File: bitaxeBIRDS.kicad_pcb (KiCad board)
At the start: 6 copper layers, 65 x 112 mm, 195 parts, among them J1 XT30, J2 USB_C_Receptacle_USB2.0, J3 Conn_01x04, J4 Conn_01x04, SW1 SWITCH-SPST, SW2 SWITCH-SPST, U1 TPSM861253RDXR, U12 TLV75512PDQNR, U13 EMC2103-2, U14 TLV75512PDQNR, U15 TLV75512PDQNR, U2 TPS546D24ARVFR, U3 TLV75512PDQNR, U4 W25Q16JVUXIQ TR, U5 TPS22919DCKR, U6 RP2040, U7 SK6812, U8 SN74AVC4T774, U9 Raspberry Pi Pico, Y1 12MHz, Y2 50MHz

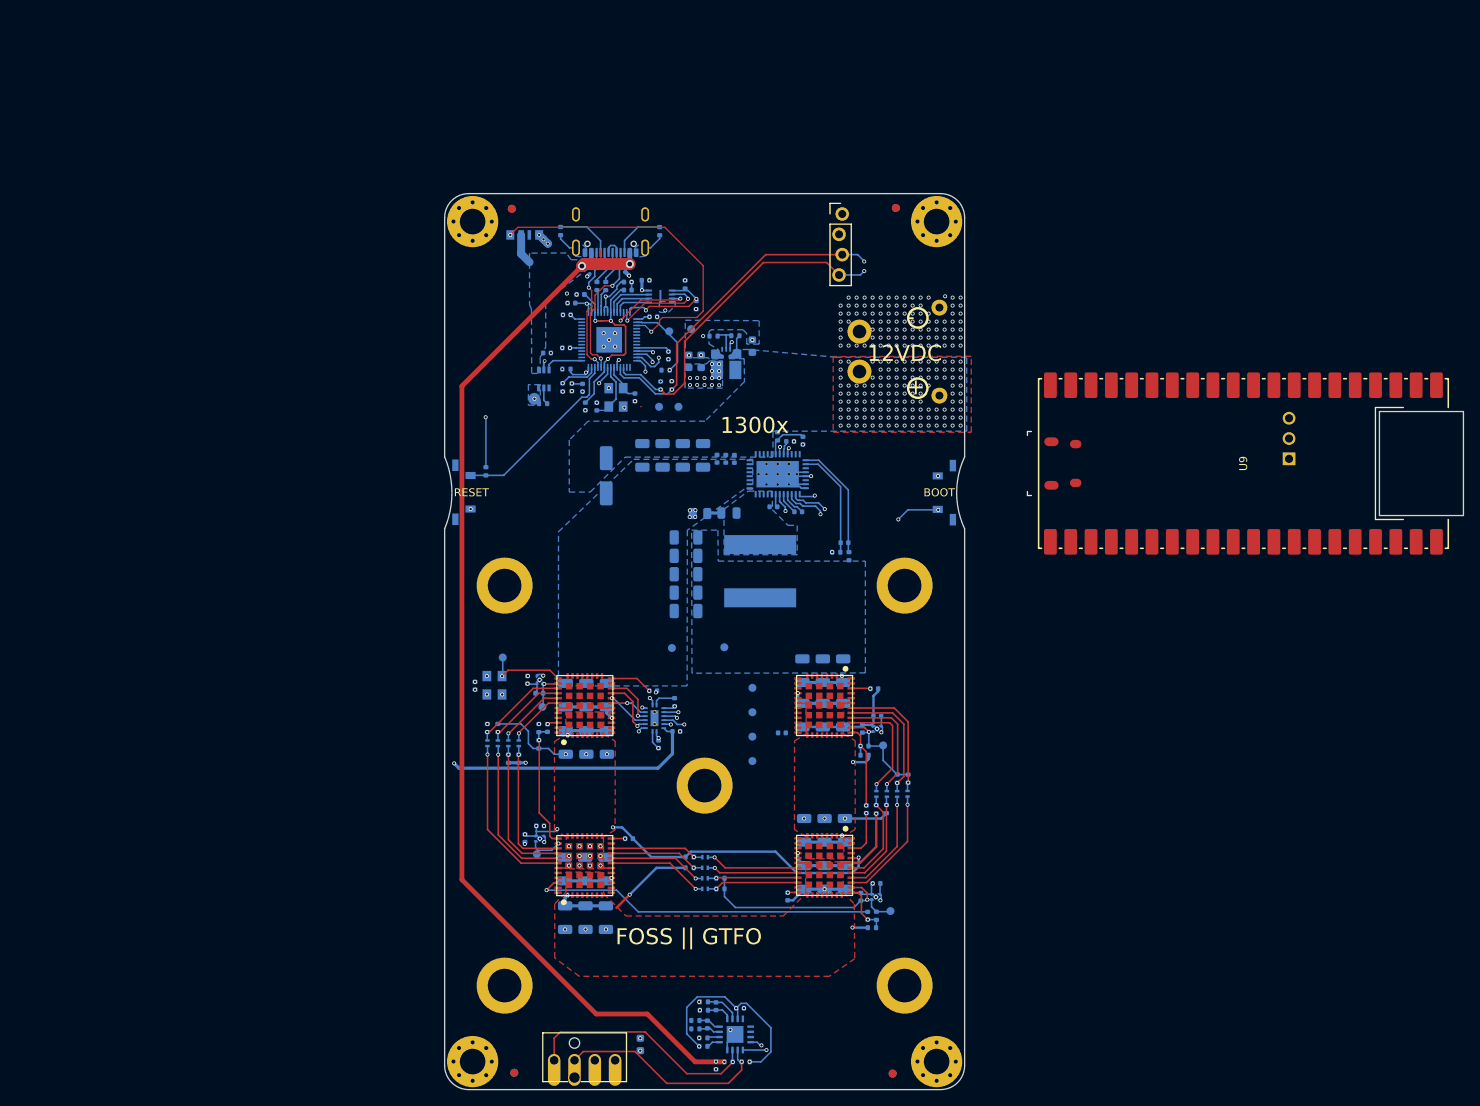
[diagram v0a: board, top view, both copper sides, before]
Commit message: switched to THT RPi Pico 2W style. Made 8mm taller.
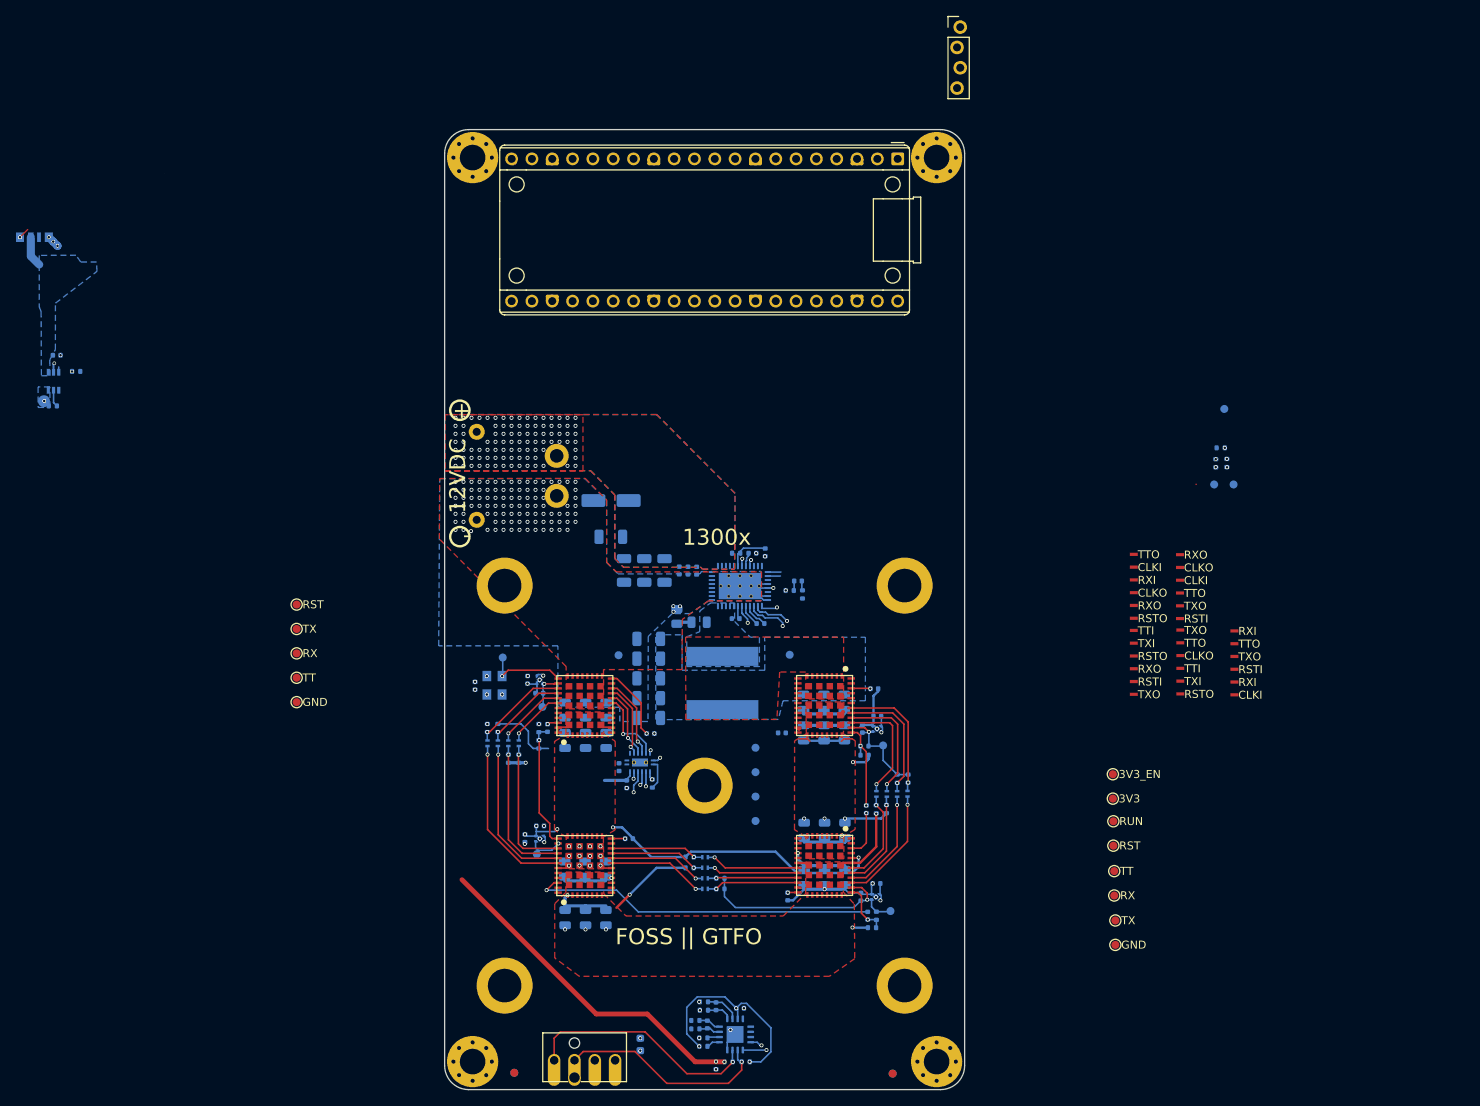
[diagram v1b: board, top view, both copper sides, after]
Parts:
- removed C1, C12, C8: 10uF, Capacitor_SMD:C_0603_1608Metric
- removed C42, C43: 30pF, Capacitor_SMD:C_0402_1005Metric
- removed C44, C46, C47, C50, C51, C52, C53, C54, C55, C56: 0.1uF, Capacitor_SMD:C_0402_1005Metric
- removed C48, C49: 1uF, Capacitor_SMD:C_0402_1005Metric
- removed J2: USB_C_Receptacle_USB2.0, aditBoard:USB_C_Receptacle_GCT_USB4105-xx-A_16P_TopMnt_Horizontal
- removed R1: 20k, Resistor_SMD:R_0402_1005Metric
- removed R15, R2, R4: 10k, Resistor_SMD:R_0402_1005Metric
- removed R16, R17: 5.1k, Resistor_SMD:R_0402_1005Metric
- removed R18: 1k, Resistor_SMD:R_0402_1005Metric
- removed R19: 49.9k, Resistor_SMD:R_0402_1005Metric
- removed R21, R22: 33, Resistor_SMD:R_0402_1005Metric
- removed SW1, SW2: SWITCH-SPST, bitaxe:SW_TL3330AF130QG_EWI
- removed U1: TPSM861253RDXR, bitaxe:TPSM863257RDX
- removed U4: W25Q16JVUXIQ TR, emberone:USON-8_UX_2x3x0p6_WIN
- removed U6: RP2040, Package_DFN_QFN:QFN-56-1EP_7x7mm_P0.4mm_EP3.2x3.2mm
- removed Y1: 12MHz, emberone:XTAL_ECS-120-20-33-CKM-TR3
- added TP15: 3V3, bitaxe:TestPoint_Pad_D1.0mm, F.Cu at (182.0, 113.6)
- added TP16: RUN, bitaxe:TestPoint_Pad_D1.0mm, F.Cu at (182.1, 116.5)
- added TP17: TX, bitaxe:TestPoint_Pad_D1.0mm, F.Cu at (80.0, 92.4)
- added TP20: RX, bitaxe:TestPoint_Pad_D1.0mm, F.Cu at (80.0, 95.5)
- added TP21: TT, bitaxe:TestPoint_Pad_D1.0mm, F.Cu at (80.0, 98.5)
- added TP22: GND, bitaxe:TestPoint_Pad_D1.0mm, F.Cu at (80.0, 101.6)
- added TP23: RST, bitaxe:TestPoint_Pad_D1.0mm, F.Cu at (182.1, 119.5)
- added TP24: TT, bitaxe:TestPoint_Pad_D1.0mm, F.Cu at (182.2, 122.7)
- added TP25: RX, bitaxe:TestPoint_Pad_D1.0mm, F.Cu at (182.2, 125.7)
- added TP26: TX, bitaxe:TestPoint_Pad_D1.0mm, F.Cu at (182.3, 128.9)
- added TP27: GND, bitaxe:TestPoint_Pad_D1.0mm, F.Cu at (182.3, 131.9)
- added TP28: TTI, bitaxe:TestPoint_Pad_1.0x0.4mm, F.Cu at (184.6, 92.6)
- added TP29: TXI, bitaxe:TestPoint_Pad_1.0x0.4mm, F.Cu at (184.6, 94.2)
- added TP30: RSTO, bitaxe:TestPoint_Pad_1.0x0.4mm, F.Cu at (184.6, 95.8)
- added TP31: RXO, bitaxe:TestPoint_Pad_1.0x0.4mm, F.Cu at (184.6, 97.4)
- added TP32: RSTI, bitaxe:TestPoint_Pad_1.0x0.4mm, F.Cu at (184.6, 99.0)
- added TP33: TXO, bitaxe:TestPoint_Pad_1.0x0.4mm, F.Cu at (184.6, 100.6)
- added TP34: TTO, bitaxe:TestPoint_Pad_1.0x0.4mm, F.Cu at (184.6, 83.1)
- added TP35: CLKI, bitaxe:TestPoint_Pad_1.0x0.4mm, F.Cu at (184.6, 84.7)
- added TP36: RXI, bitaxe:TestPoint_Pad_1.0x0.4mm, F.Cu at (184.6, 86.3)
- added TP37: CLKO, bitaxe:TestPoint_Pad_1.0x0.4mm, F.Cu at (184.6, 87.9)
- added TP38: RXO, bitaxe:TestPoint_Pad_1.0x0.4mm, F.Cu at (184.6, 89.5)
- added TP39: RSTO, bitaxe:TestPoint_Pad_1.0x0.4mm, F.Cu at (184.6, 91.1)
- added TP40: TXO, bitaxe:TestPoint_Pad_1.0x0.4mm, F.Cu at (190.5, 92.6)
- added TP41: TTO, bitaxe:TestPoint_Pad_1.0x0.4mm, F.Cu at (190.5, 94.2)
- added TP42: CLKO, bitaxe:TestPoint_Pad_1.0x0.4mm, F.Cu at (190.5, 95.7)
- added TP43: TTI, bitaxe:TestPoint_Pad_1.0x0.4mm, F.Cu at (190.5, 97.3)
- added TP44: TXI, bitaxe:TestPoint_Pad_1.0x0.4mm, F.Cu at (190.5, 98.9)
- added TP45: RSTO, bitaxe:TestPoint_Pad_1.0x0.4mm, F.Cu at (190.5, 100.5)
- added TP46: RXO, bitaxe:TestPoint_Pad_1.0x0.4mm, F.Cu at (190.4, 83.1)
- added TP47: CLKO, bitaxe:TestPoint_Pad_1.0x0.4mm, F.Cu at (190.4, 84.7)
- added TP48: CLKI, bitaxe:TestPoint_Pad_1.0x0.4mm, F.Cu at (190.4, 86.3)
- added TP49: TTO, bitaxe:TestPoint_Pad_1.0x0.4mm, F.Cu at (190.4, 87.9)
- added TP5: 3V3_EN, bitaxe:TestPoint_Pad_D1.0mm, F.Cu at (182.0, 110.6)
- added TP50: TXO, bitaxe:TestPoint_Pad_1.0x0.4mm, F.Cu at (190.4, 89.5)
- added TP51: RSTI, bitaxe:TestPoint_Pad_1.0x0.4mm, F.Cu at (190.4, 91.1)
- added TP52: RXI, bitaxe:TestPoint_Pad_1.0x0.4mm, F.Cu at (197.2, 92.7)
- added TP53: TTO, bitaxe:TestPoint_Pad_1.0x0.4mm, F.Cu at (197.2, 94.3)
- added TP54: TXO, bitaxe:TestPoint_Pad_1.0x0.4mm, F.Cu at (197.2, 95.9)
- added TP55: RSTI, bitaxe:TestPoint_Pad_1.0x0.4mm, F.Cu at (197.2, 97.5)
- added TP56: RXI, bitaxe:TestPoint_Pad_1.0x0.4mm, F.Cu at (197.2, 99.1)
- added TP57: CLKI, bitaxe:TestPoint_Pad_1.0x0.4mm, F.Cu at (197.2, 100.7)
- C100, C101, C107, C108, C109, C115, C116, C117, C123, C124, C125, C131, C132, C133, C139, C140, C141, C83, C84, C85, C91, C92, C93, C99: footprint Capacitor_SMD:C_1206_3216Metric -> Capacitor_SMD:C_0805_2012Metric
- TP14: value TRP -> TT
- TP6: value GND -> RST; moved to F.Cu
- U9: footprint bitaxe:RasPi_Pico_W_SMD -> bitaxe:RaspberryPi_Pico_Common_THT
- moved U9 73.4 mm to (131.0, 42.5), turned to -90 degrees
- moved TP1 70.1 mm to (196.0, 64.9)
- moved R23 70.1 mm to (194.9, 71.7)
- moved R24 70.1 mm to (196.3, 71.7)
- moved TP8 70.1 mm to (197.1, 74.4)
- moved TP9 70.1 mm to (194.7, 74.4)
- moved R3 70.1 mm to (195.5, 69.8)
- moved C45 61.3 mm to (50.0, 58.2)
- moved R25 61.3 mm to (52.4, 60.2)
- moved U5 61.3 mm to (49.6, 61.5)
- moved U7 61.3 mm to (47.2, 43.5)
- moved R20 61.3 mm to (49.5, 64.5)
- moved TP6 60.1 mm to (80.0, 89.4), turned to 0 degrees
- moved J1 40.9 mm to (112.5, 73.3), turned to -90 degrees
- moved J3 27.6 mm to (162.8, 17.2)
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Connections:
- A1 pad 31: /ASIC/shifter1-2/TRIP_IN -> /ASIC/shifter1-2/RX_OUT
- A1 pad 32: /ASIC/shifter1-2/TX_IN -> /ASIC/shifter1-2/RESET_OUT
- A1 pad 33: /ASIC/shifter1-2/RESET_OUT -> /ASIC/shifter1-2/TX_IN
- A1 pad 34: /ASIC/shifter1-2/RX_OUT -> /ASIC/shifter1-2/TRIP_IN
- A2 pad 31: /ASIC/shifter1-2/RX_IN -> /ASIC/shifter1-2/TRIP_OUT
- A2 pad 32: /ASIC/shifter1-2/RESET_IN -> /ASIC/shifter1-2/TX_OUT
- A2 pad 33: /ASIC/shifter1-2/TX_OUT -> /ASIC/shifter1-2/RESET_IN
- A2 pad 34: /ASIC/shifter1-2/TRIP_OUT -> /ASIC/shifter1-2/RX_IN
- R25 pad 1: /Power/SMB_ALRT -> /Power/PGOOD
- TP6 pad 1: GND -> /ASIC/RST_1V2
- U7 pad 1: Net-(U6-GPIO1) -> Net-(U7-DIN)
- U9 pad 1: unconnected-(U9-GP0-Pad1) -> /Power/PWR_EN
- U9 pad 11: unconnected-(U9-GP8-Pad11) -> /ASIC/RX_3V3
- U9 pad 12: unconnected-(U9-GP9-Pad12) -> /ASIC/TX_3V3
- U9 pad 13: unconnected-(U9-GND-Pad13) -> GND
- U9 pad 14: unconnected-(U9-GP10-Pad14) -> /ASIC/TRIP_3V3
- U9 pad 15: unconnected-(U9-GP11-Pad15) -> /ASIC/RST_3V3
- U9 pad 18: unconnected-(U9-GND-Pad18) -> GND
- U9 pad 19: unconnected-(U9-GP14-Pad19) -> /Data/SDA
- U9 pad 2: unconnected-(U9-GP1-Pad2) -> Net-(U7-DIN)
- U9 pad 20: unconnected-(U9-GP15-Pad20) -> /Data/SCL
- U9 pad 21: unconnected-(U9-GP16-Pad21) -> /Power/PGOOD
- U9 pad 22: unconnected-(U9-GP17-Pad22) -> /Power/SMB_ALRT
- U9 pad 23: unconnected-(U9-GND-Pad23) -> GND
- U9 pad 24: unconnected-(U9-GP18-Pad24) -> /Data/5V_EN
- U9 pad 28: unconnected-(U9-GND-Pad28) -> GND
- U9 pad 3: unconnected-(U9-GND-Pad3) -> GND
- U9 pad 30: unconnected-(U9-RUN-Pad30) -> Net-(U9-RUN)
- U9 pad 31: unconnected-(U9-GP26_A0-Pad31) -> /ASIC/GND2
- U9 pad 32: unconnected-(U9-GP27_A1-Pad32) -> /ASIC/GND3
- U9 pad 33: unconnected-(U9-AGND-Pad33) -> GND
- U9 pad 34: unconnected-(U9-GP28_A2-Pad34) -> /ASIC/GND4
- U9 pad 36: unconnected-(U9-3V3-Pad36) -> /3V3
- U9 pad 37: unconnected-(U9-3V3_EN-Pad37) -> Net-(U9-3V3_EN)
- U9 pad 38: unconnected-(U9-GND-Pad38) -> GND
- U9 pad 39: unconnected-(U9-VSYS-Pad39) -> /5V
- U9 pad 40: unconnected-(U9-VBUS-Pad40) -> /5V
- U9 pad 8: unconnected-(U9-GND-Pad8) -> GND
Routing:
- net /3V3: track 206.2 -> 86.4 mm, vias 33 -> 6
- net /5V: track 140.1 -> 46.1 mm, vias 4 -> 2
- net /Data/SCL: track 177.9 -> 87.3 mm, vias 4 -> 3
- net /Data/SDA: track 176.0 -> 89.0 mm, vias 4 -> 3
- net /ASIC/TRIP_3V3: track 61.9 -> 1.83 mm, vias 2 -> 1
- net /ASIC/RX_3V3: track 60.9 -> 1.74 mm, vias 2 -> 1
- net /ASIC/TX_3V3: track 61.3 -> 2.79 mm, vias 2 -> 1
- net /Power/PGOOD: track 60.0 -> 1.80 mm, vias 2 -> 1
- net /ASIC/RST_3V3: track 58.3 -> 0.91 mm, vias 2 -> 1
- net /Power/SMB_ALRT: track 57.7 -> 2.43 mm, vias 2 -> 1
- net /Data/MCU_BOOT: track 55.1 -> 0.00 mm, vias 3 -> 0
- net Net-(U6-GPIO1): track 42.1 -> 0.00 mm, vias 2 -> 0
- net /5V_SWITCH: track 177.9 -> 139.6 mm
- net /Power/PWR_EN: track 28.8 -> 0.93 mm, vias 3 -> 2
- net /Data/1V1: track 26.2 -> 0.00 mm, vias 3 -> 0
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- added copper zone on In2.Cu, net /12V
- added copper zone on F.Cu, net /VDD
- added copper zone on F.Cu, net GND
- removed copper zone on B.Cu, net /3V3
- removed copper zone on In2.Cu, net /3V3
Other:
- board size 65 x 112 mm -> 65 x 120 mm
- board text removed: "BOOT"
- board text removed: "RESET"

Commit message: lots of routing
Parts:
- removed J3: Conn_01x04, bitaxe:PinHeader_1x04_P2.54mm_Vertical_shifted
- removed U7: SK6812, emberone:LED-SMD_4P-L4.0-W1.6-L
- TP11: value RX -> TTI; footprint bitaxe:TestPoint_Pad_D1.0mm -> bitaxe:TestPoint_Pad_1.0x0.4mm; moved to F.Cu
- TP12: value RST -> TXI; footprint bitaxe:TestPoint_Pad_D1.0mm -> bitaxe:TestPoint_Pad_1.0x0.4mm; moved to F.Cu
- TP13: value TX -> RSTI; footprint bitaxe:TestPoint_Pad_D1.0mm -> bitaxe:TestPoint_Pad_1.0x0.4mm; moved to F.Cu
- TP14: value TT -> RXO; footprint bitaxe:TestPoint_Pad_D1.0mm -> bitaxe:TestPoint_Pad_1.0x0.4mm; moved to F.Cu
- TP15, TP16, TP23, TP24, TP25, TP26, TP27, TP5: moved to B.Cu
- TP17: value TX -> TXO; footprint bitaxe:TestPoint_Pad_D1.0mm -> bitaxe:TestPoint_Pad_1.0x0.4mm
- TP20: value RX -> RXI; footprint bitaxe:TestPoint_Pad_D1.0mm -> bitaxe:TestPoint_Pad_1.0x0.4mm
- TP21: value TT -> TTO; footprint bitaxe:TestPoint_Pad_D1.0mm -> bitaxe:TestPoint_Pad_1.0x0.4mm
- TP22: footprint bitaxe:TestPoint_Pad_D1.0mm -> bitaxe:TestPoint_Pad_1.0x0.4mm
- TP6: value RST -> RSTI; footprint bitaxe:TestPoint_Pad_D1.0mm -> bitaxe:TestPoint_Pad_1.0x0.4mm
- moved TP27 100.9 mm to (134.5, 43.0), turned to 90 degrees
- moved U5 99.5 mm to (149.2, 61.3)
- moved R20 99.5 mm to (149.1, 64.4)
- moved C45 99.3 mm to (149.3, 58.1)
- moved TP26 96.8 mm to (137.5, 43.0), turned to 90 degrees
- moved J4 95.6 mm to (159.8, 61.3), turned to -90 degrees
- moved TP25 92.4 mm to (140.6, 43.2), turned to 90 degrees
- moved C76 91.5 mm to (155.1, 58.7), turned to 90 degrees
- moved TP24 88.3 mm to (143.7, 43.2), turned to 90 degrees
- moved TP36 87.3 mm to (103.3, 117.9), turned to 90 degrees
- moved C77 86.7 mm to (140.5, 60.6), turned to 90 degrees
- moved R34 85.6 mm to (139.0, 61.1), turned to 0 degrees
- moved R33 85.5 mm to (136.8, 61.1), turned to 180 degrees
- moved TP34 84.8 mm to (107.3, 117.9), turned to 90 degrees
- moved TP23 84.0 mm to (146.9, 43.3), turned to 90 degrees
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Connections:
- TP11 pad 1: Net-(A4-RX_OUT) -> Net-(A4-TRIP_IN)
- TP12 pad 1: Net-(A4-RESET_OUT) -> Net-(A4-TX_IN)
- TP13 pad 1: Net-(A4-TX_IN) -> Net-(A4-RESET_OUT)
- TP14 pad 1: Net-(A4-TRIP_IN) -> Net-(A4-RX_OUT)
- U9 pad 1: /Power/PWR_EN -> unconnected-(U9-GP0-Pad1)
- U9 pad 2: Net-(U7-DIN) -> unconnected-(U9-GP1-Pad2)
- U9 pad 25: unconnected-(U9-GP19-Pad25) -> /Power/PWR_EN
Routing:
- net /ASIC/RST_3V3: track 0.91 -> 112.2 mm, vias 1 -> 2
- net /ASIC/TX_3V3: track 2.79 -> 105.7 mm, vias 1 -> 2
- net /ASIC/TRIP_3V3: track 1.83 -> 100.9 mm
- net /ASIC/RX_3V3: track 1.74 -> 98.8 mm
- net /12V: track 111.8 -> 49.8 mm, vias 96 -> 118
- net /Power/SMB_ALRT: track 2.43 -> 59.8 mm
- net /Power/PGOOD: track 1.80 -> 53.6 mm
- net /5V_SWITCH: track 139.6 -> 187.3 mm, vias 7 -> 12
- net /ASIC/1V2-1: track 15.6 -> 57.4 mm, vias 5 -> 6
- net /Power/PWR_EN: track 0.93 -> 41.9 mm
- net /Data/5V_EN: track 0.67 -> 39.7 mm, vias 0 -> 2
- net /5V: track 46.1 -> 23.0 mm
- net /ASIC/RST_1V2: track 9.27 -> 24.9 mm
- net /ASIC/TX_1V2: track 8.65 -> 23.2 mm
- net /ASIC/RX_1V2: track 10.1 -> 23.9 mm
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- added copper zone on B.Cu, net /ASIC/GND2
- added copper zone on In2.Cu, net /ASIC/GND2
- added copper zone on B.Cu, net /ASIC/GND3
- added copper zone on In2.Cu, net /ASIC/GND3
- added copper zone on B.Cu, net /ASIC/GND4
- added copper zone on In2.Cu, net /ASIC/GND4
- added copper zone on F.Cu, net /Power/SW1
- removed copper zone on B.Cu, net /5V
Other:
- board text removed: "3V3"
- board text removed: "GND"
- board text removed: "LFG"
- board text removed: "SCL"
- board text removed: "SDA"

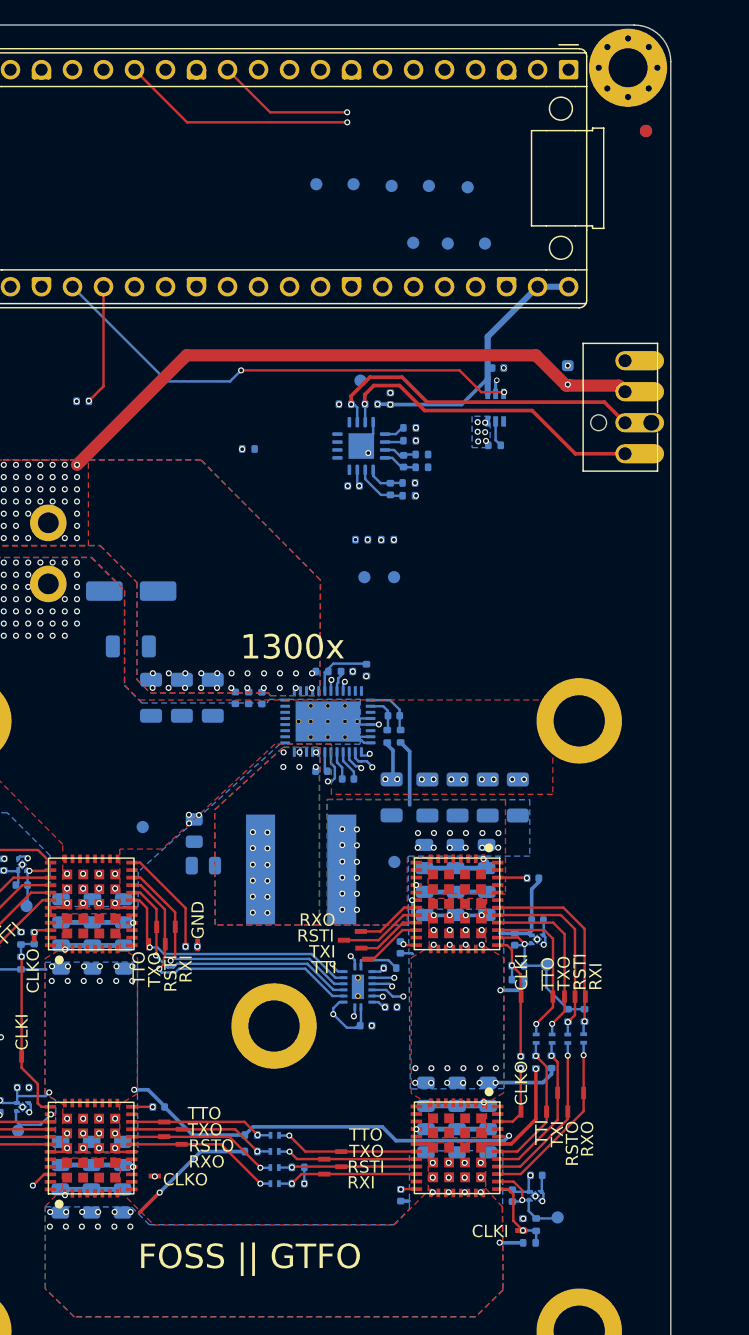
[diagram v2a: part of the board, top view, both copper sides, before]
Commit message: routing done, needs DRC and cleanup
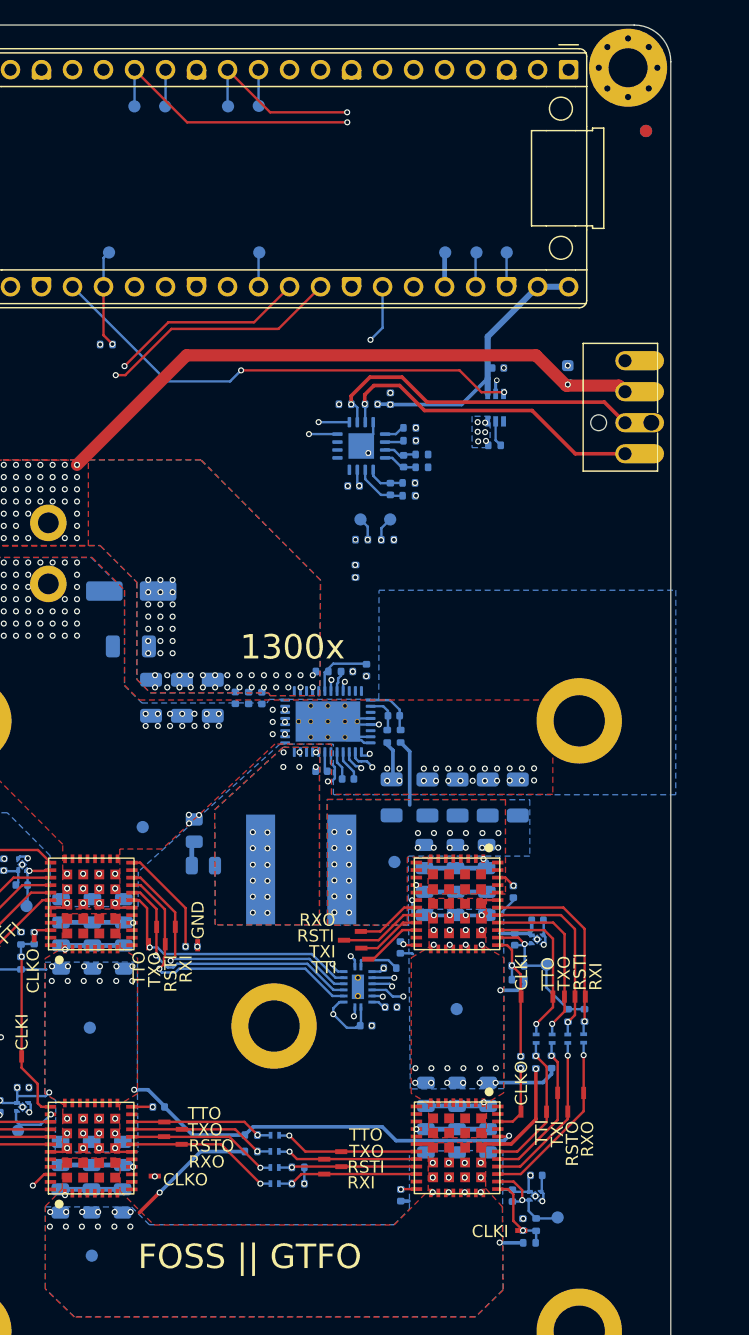
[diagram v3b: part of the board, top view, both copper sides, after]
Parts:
- added TP58: D1, bitaxe:TestPoint_Pad_D1.0mm, B.Cu at (115.9, 112.1)
- added TP59: D2, bitaxe:TestPoint_Pad_D1.0mm, B.Cu at (116.1, 130.8)
- added TP60: D3, bitaxe:TestPoint_Pad_D1.0mm, B.Cu at (146.0, 110.6)
- moved TP23 28.1 mm to (119.6, 36.7), turned to -90 degrees
- moved TP1 23.1 mm to (117.5, 48.6)
- moved TP24 22.6 mm to (122.1, 36.7), turned to -90 degrees
- moved TP27 16.6 mm to (150.1, 48.6)
- moved R25 13.3 mm to (137.7, 74.7), turned to 90 degrees
- moved TP25 12.7 mm to (129.8, 36.6), turned to -90 degrees
- moved TP16 12.6 mm to (129.8, 48.6)
- moved TP26 12.1 mm to (127.2, 36.7), turned to -90 degrees
- moved TP8 5.47 mm to (138.1, 70.5), turned to 0 degrees
- moved TP9 5.18 mm to (140.5, 70.5), turned to 0 degrees
- moved R3 5.03 mm to (117.3, 56.2)
- moved C60 1.96 mm to (150.6, 101.0), turned to -90 degrees
- moved TP5 1.01 mm to (147.6, 48.6)
- moved TP15 0.76 mm to (145.0, 48.6)
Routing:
- net /ASIC/GND3: track 29.1 -> 121.3 mm, vias 29 -> 30
- net /ASIC/GND2: track 50.4 -> 118.3 mm, vias 30 -> 31
- net /ASIC/GND4: track 23.8 -> 80.1 mm, vias 27 -> 28
- net /5V_SWITCH: track 187.3 -> 206.5 mm
- net /3V3: track 93.1 -> 110.3 mm
- net /Power/PGOOD: track 53.6 -> 58.6 mm, vias 1 -> 2
- net /Power/SMB_ALRT: track 59.8 -> 63.7 mm
- net /ASIC/TX_3V3: track 105.7 -> 108.7 mm
- net /ASIC/TRIP_3V3: track 100.9 -> 103.9 mm
- net /ASIC/RST_3V3: track 112.2 -> 115.2 mm
- net /ASIC/RX_3V3: track 98.8 -> 101.8 mm
- net Net-(U9-3V3_EN): track 0.00 -> 2.84 mm
- net Net-(U9-RUN): track 0.00 -> 2.83 mm
- net GND: track 29.2 -> 31.8 mm, vias 142 -> 177
- net /Power/PWR_EN: track 41.9 -> 44.4 mm
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- added copper zone on In2.Cu, net /Power/SW1
- added copper zone on In2.Cu, net /VDD
